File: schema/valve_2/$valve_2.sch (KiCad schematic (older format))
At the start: 119 parts, among them J1 DB37, J2 DB37, J3 DB9, K1 i2c-1, K2 i2c-2, P1 SETUP, P2 power-1, P3 power-2, P4 SWD-IAP, U1 74HC165, U10 L293, U11 L293, U12 L293, U13 L293, U14 MINI-USB-B, U15 NCP3063, U16 NCP3063, U2 74HC165, U3 74HC164, U4 74HC164, U5 74HC164, U6 74HC164, U7 L293, U8 L293, U9 L293, X1 8MHz

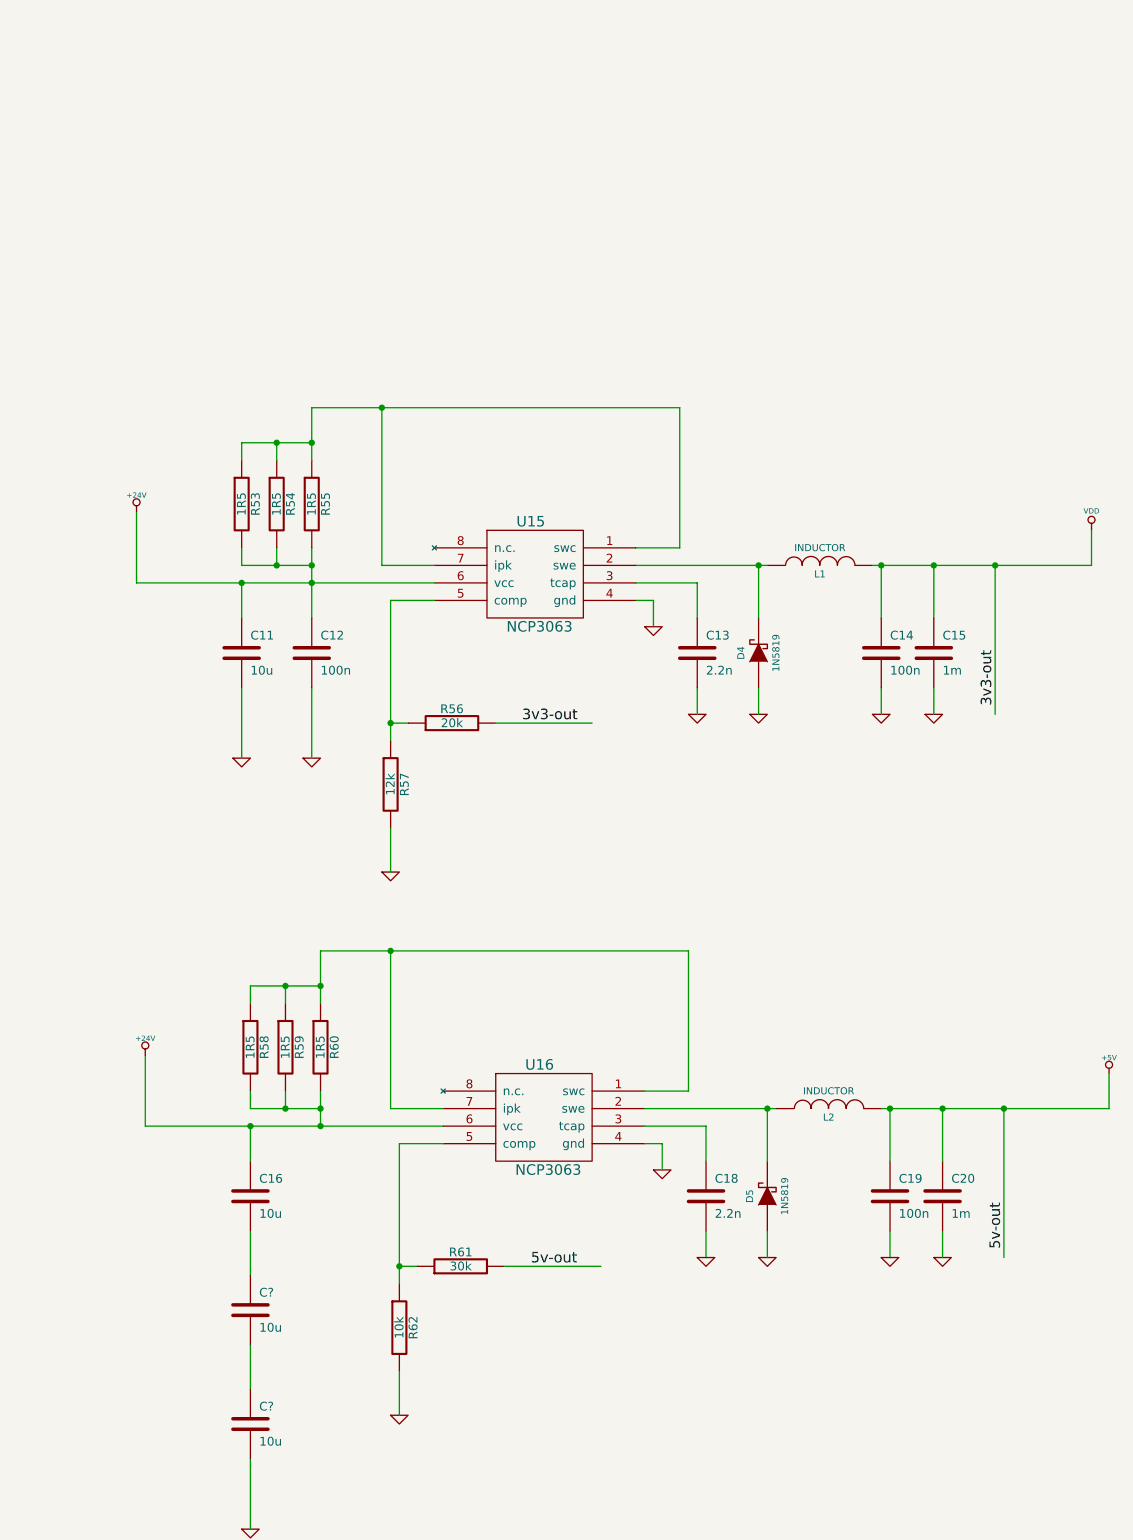
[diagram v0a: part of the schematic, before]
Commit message: Made separate I2C sockets couple close to MCU to minimize cross currents from other PCB parts.
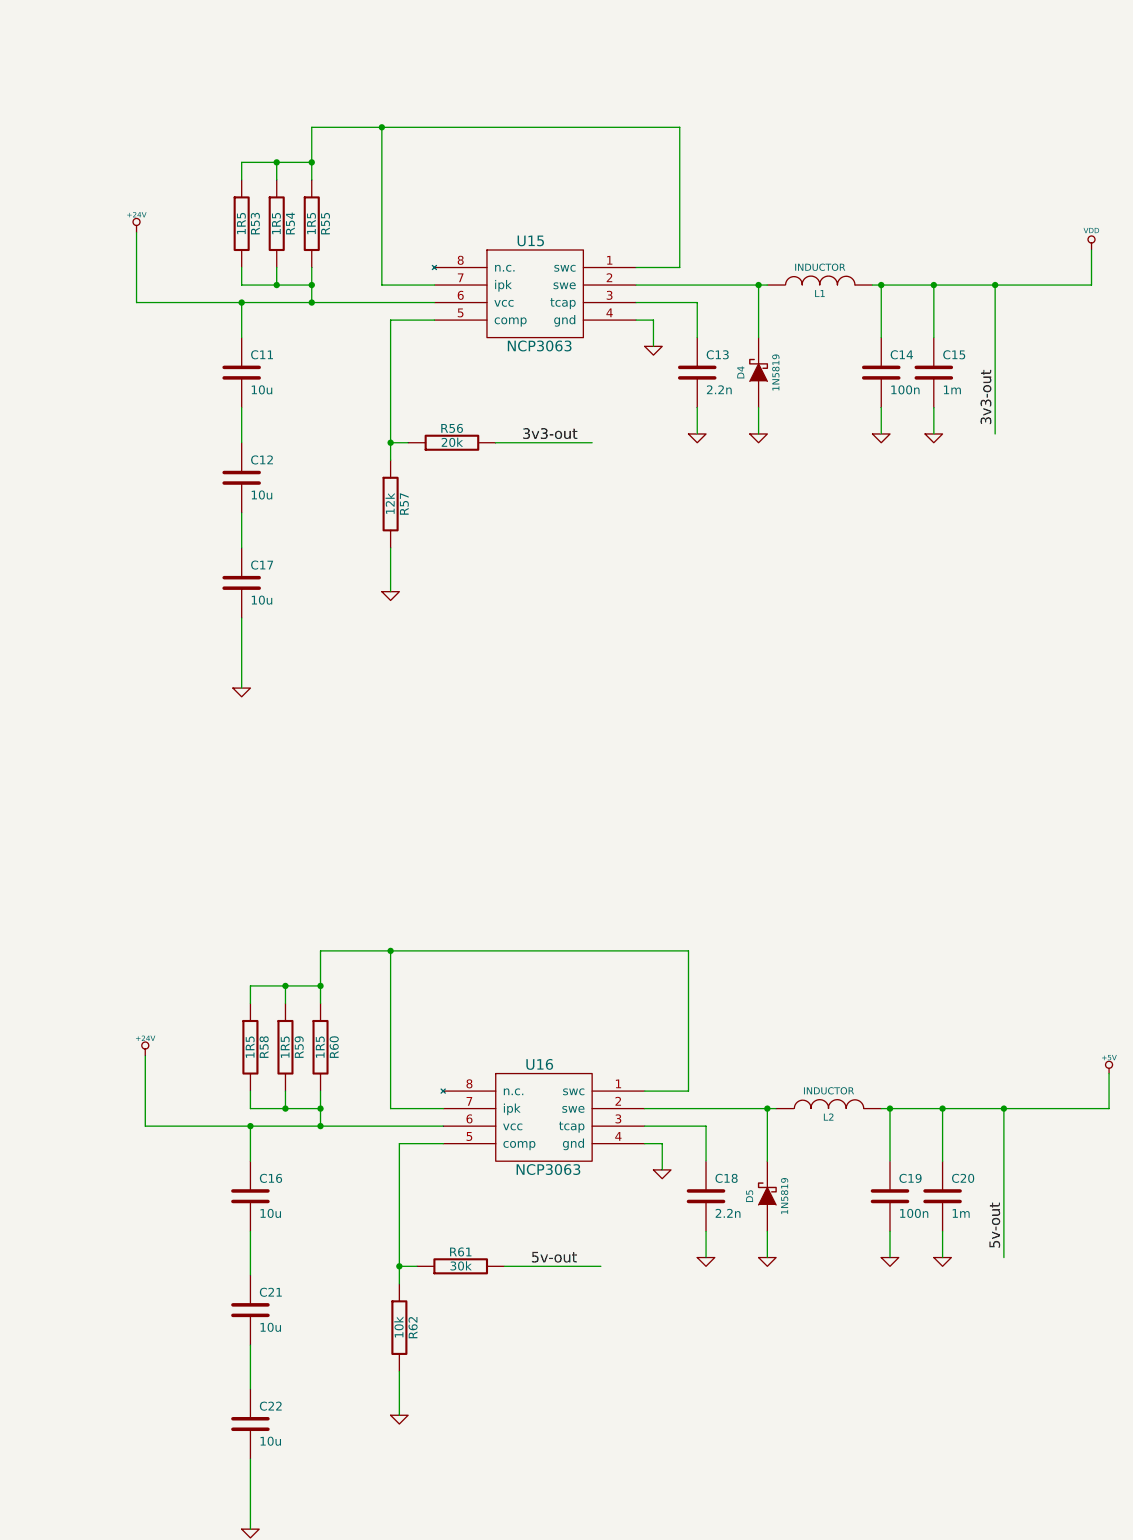
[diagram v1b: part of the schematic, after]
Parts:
- added C17: 10u, symbol C
- C12: value 100n -> 10u
- gave numbers to parts that had none: 2
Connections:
- wire segments 688 -> 689
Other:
- moved on the sheet: C11, C13, C14, C15, D4, L1, R53, R54, R55, R56, R57, U15
